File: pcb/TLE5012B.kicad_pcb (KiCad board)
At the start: 2 copper layers, 35 x 35 mm, 14 parts, among them J1 Conn_02x6_Odd_Even, J2 Conn_01x4, U1 ME6211C33M5G-N, U2 TLE5012B

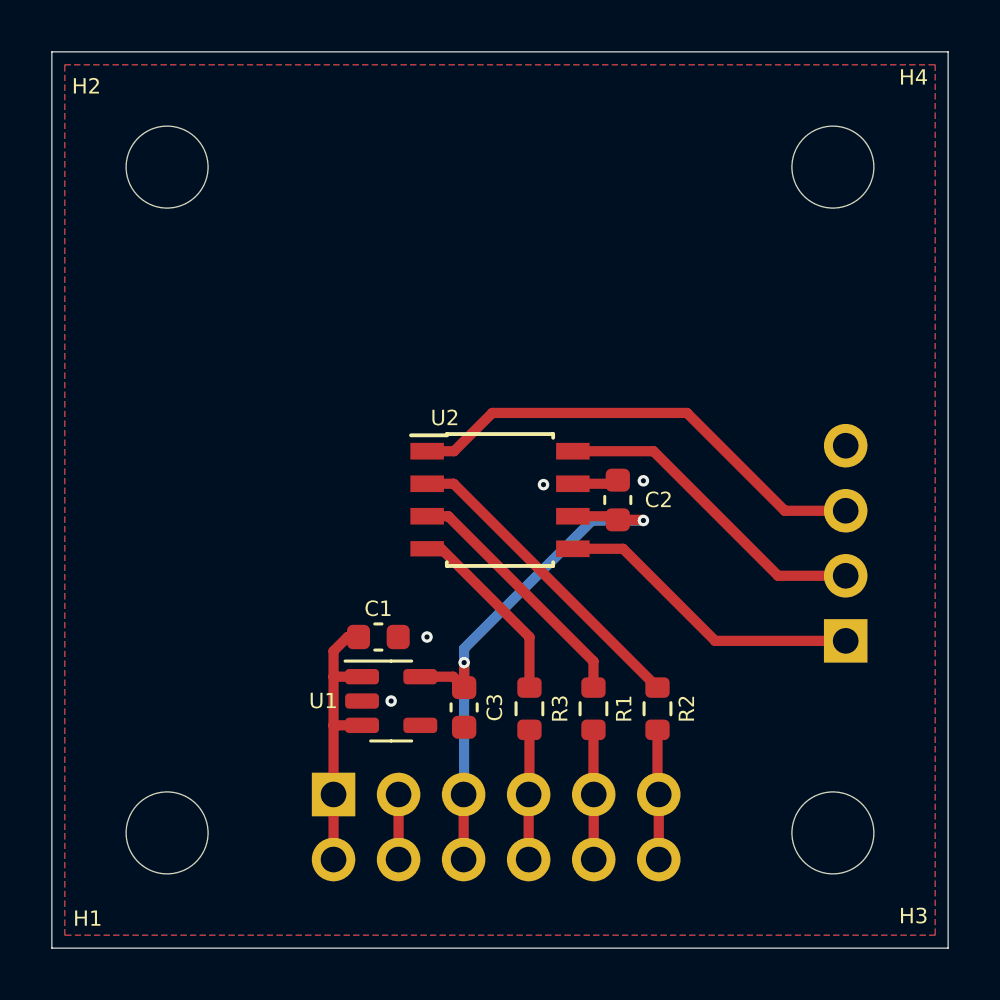
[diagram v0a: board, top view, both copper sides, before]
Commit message: pcb: Minor updates to pcb
Only have one CS pin header (ground the others).
Add additional ground vias around perimeter of board.
Update 100nF LCSC part number
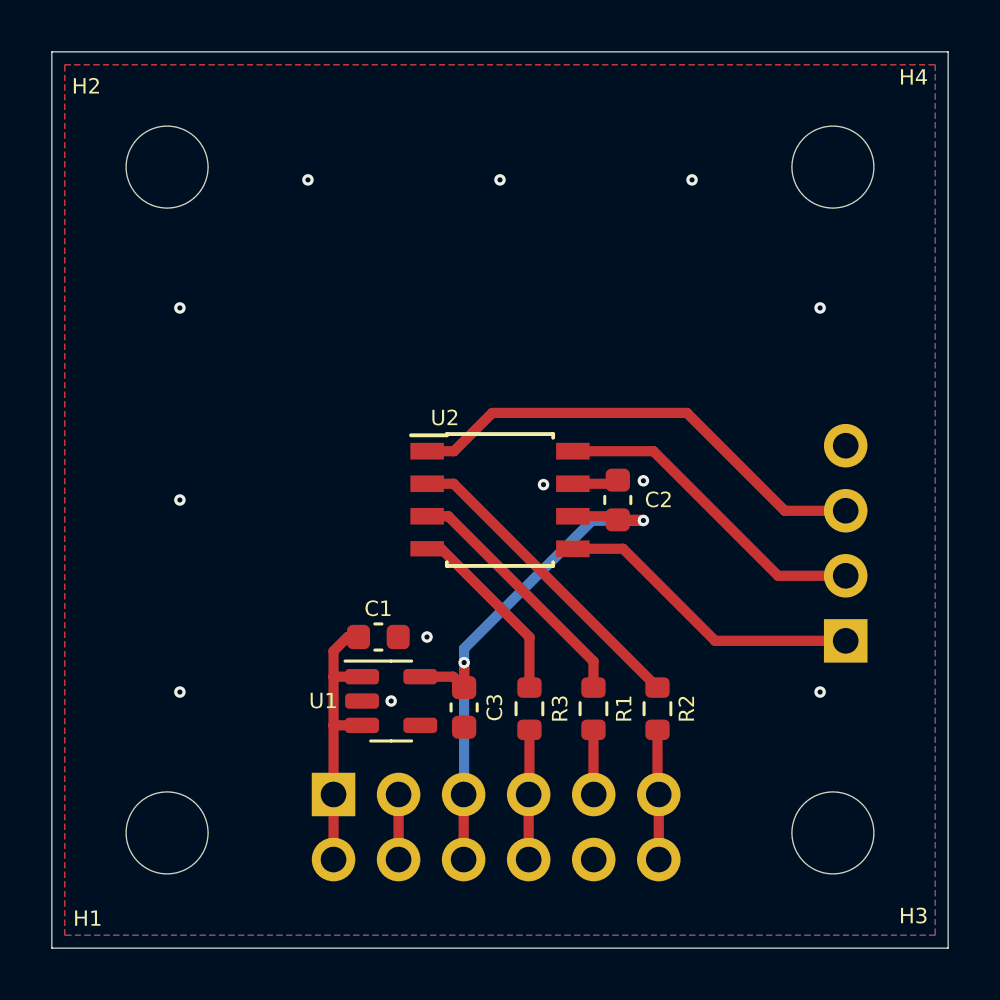
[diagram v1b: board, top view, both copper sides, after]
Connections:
- J1 pad 10: CS_SPI -> GND
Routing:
- net CS_SPI: track 5.07 -> 2.53 mm
- net GND: vias 4 -> 12
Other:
- board text added: "NEMA14TLE-v0.3"
